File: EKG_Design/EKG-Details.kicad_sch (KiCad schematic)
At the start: 45 parts, among them J101 Conn_01x02_Pin, J102 Conn_01x02_Pin, J103 Conn_01x02_Pin, J104 Conn_01x03_Pin, J105 Conn_01x02_Pin, U101 OPA2156xDGK, U102 OPA2156xDGK, U103 INA826AIDR_/_SOIC8, U104 OPA2156xDGK, U105 OPA2156xDGK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

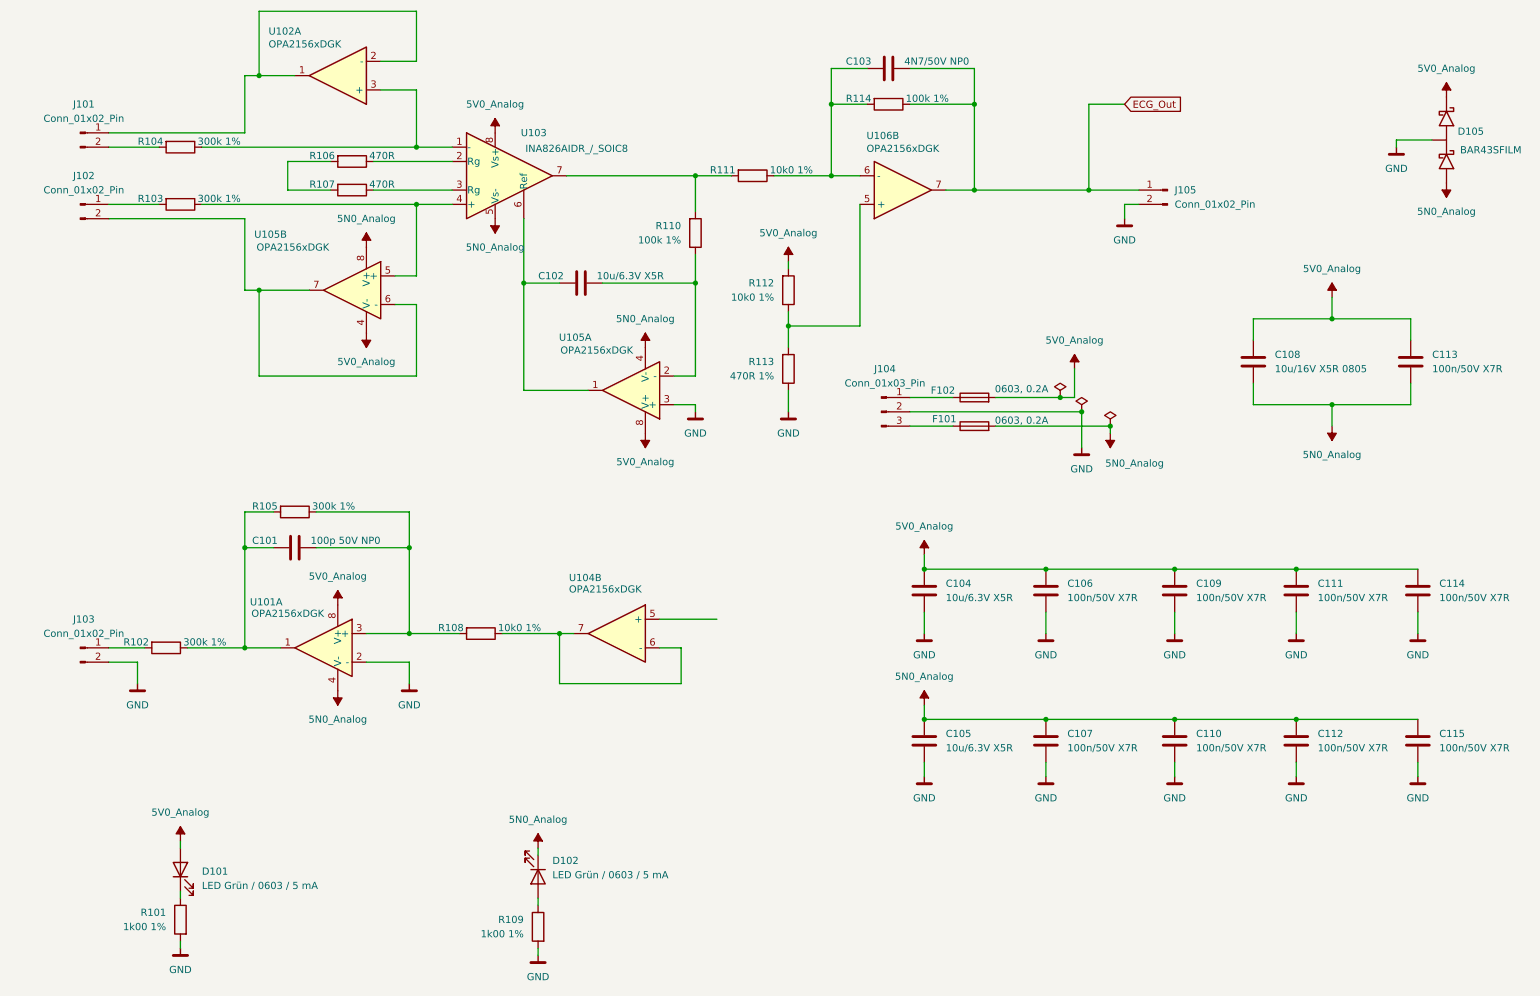
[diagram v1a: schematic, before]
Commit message: Finished ECG Schematic and finished laying out the PCB
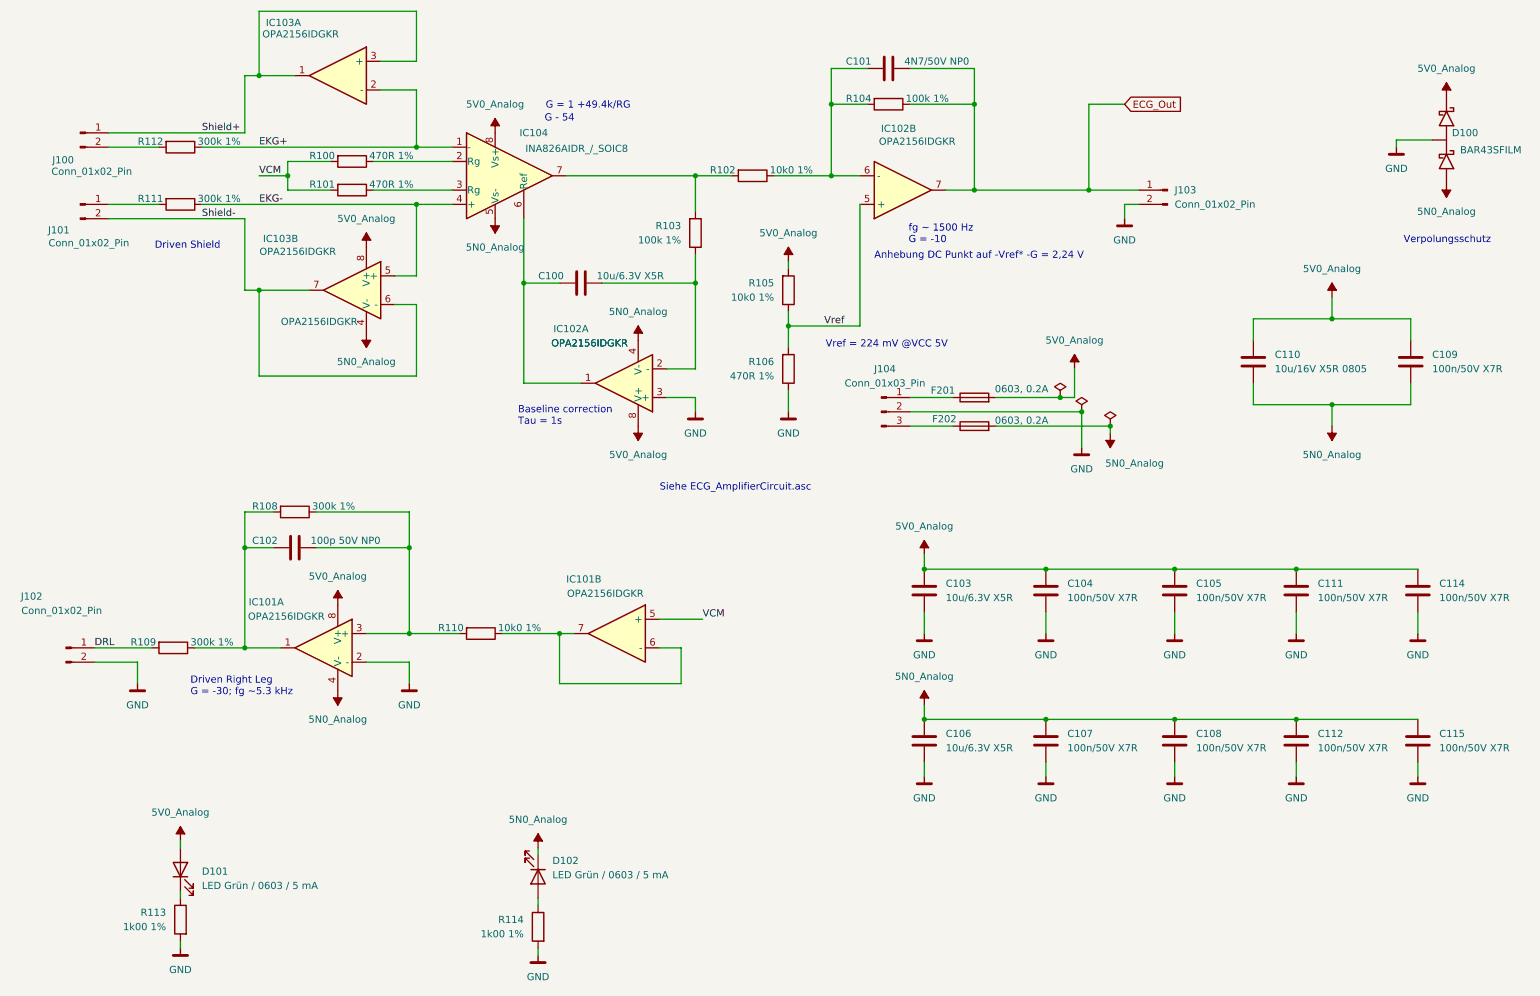
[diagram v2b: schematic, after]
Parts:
- removed unit 3 of U101
- removed unit 3 of U102
- removed U104, U106: OPA2156xDGK, Package_SO:VSSOP-8_3x3mm_P0.65mm, symbol Amplifier_Operational:OPA2156xDGK
- removed unit 3 of U105
- removed unit 2 of U105
- C100: renamed from C102; footprint (none) -> Capacitor_SMD:C_0603_1608Metric_Pad1.08x0.95mm_HandSolder
- C101: renamed from C103; footprint (none) -> Capacitor_SMD:C_0603_1608Metric_Pad1.08x0.95mm_HandSolder
- C102: renamed from C101; footprint (none) -> Capacitor_SMD:C_0603_1608Metric_Pad1.08x0.95mm_HandSolder
- C103: renamed from C104; footprint (none) -> Capacitor_SMD:C_0603_1608Metric_Pad1.08x0.95mm_HandSolder
- C104: renamed from C106; footprint (none) -> Capacitor_SMD:C_0603_1608Metric_Pad1.08x0.95mm_HandSolder
- C105: renamed from C109; footprint (none) -> Capacitor_SMD:C_0603_1608Metric_Pad1.08x0.95mm_HandSolder
- C106: renamed from C105; footprint (none) -> Capacitor_SMD:C_0603_1608Metric_Pad1.08x0.95mm_HandSolder
- C107, C111, C112, C114, C115: footprint (none) -> Capacitor_SMD:C_0603_1608Metric_Pad1.08x0.95mm_HandSolder
- C108: renamed from C110; footprint (none) -> Capacitor_SMD:C_0603_1608Metric_Pad1.08x0.95mm_HandSolder
- C109: renamed from C113; footprint (none) -> Capacitor_SMD:C_0603_1608Metric_Pad1.08x0.95mm_HandSolder
- C110: renamed from C108; footprint (none) -> Capacitor_SMD:C_0603_1608Metric_Pad1.08x0.95mm_HandSolder
- D101, D102: footprint (none) -> LED_SMD:LED_0603_1608Metric_Pad1.05x0.95mm_HandSolder
- F201: renamed from F102; footprint (none) -> Fuse:Fuse_0603_1608Metric_Pad1.05x0.95mm_HandSolder
- F202: renamed from F101; footprint (none) -> Fuse:Fuse_0603_1608Metric_Pad1.05x0.95mm_HandSolder
- IC101: renamed from U101; value OPA2156xDGK -> OPA2156IDGKR
- IC102: renamed from U105; value OPA2156xDGK -> OPA2156IDGKR
- IC103: renamed from U102; value OPA2156xDGK -> OPA2156IDGKR
- J100: renamed from J101; footprint (none) -> Connector_PinHeader_2.54mm:PinHeader_1x02_P2.54mm_Vertical
- J101: renamed from J102; footprint (none) -> Connector_PinHeader_2.54mm:PinHeader_1x02_P2.54mm_Vertical
- J102: renamed from J103; footprint (none) -> Connector_PinHeader_2.54mm:PinHeader_1x02_P2.54mm_Vertical
- J103: renamed from J105; footprint (none) -> Connector_PinHeader_2.54mm:PinHeader_1x02_P2.54mm_Vertical
- J104: footprint (none) -> Connector_PinHeader_2.54mm:PinHeader_1x03_P2.54mm_Vertical
- R100: renamed from R106; value 470R -> 470R 1%; footprint (none) -> Resistor_SMD:R_0603_1608Metric_Pad0.98x0.95mm_HandSolder
- R101: renamed from R107; value 470R -> 470R 1%; footprint (none) -> Resistor_SMD:R_0603_1608Metric_Pad0.98x0.95mm_HandSolder
- R102: renamed from R111; footprint (none) -> Resistor_SMD:R_0603_1608Metric_Pad0.98x0.95mm_HandSolder
- R103: renamed from R110; footprint (none) -> Resistor_SMD:R_0603_1608Metric_Pad0.98x0.95mm_HandSolder
- R104: renamed from R114; footprint (none) -> Resistor_SMD:R_0603_1608Metric_Pad0.98x0.95mm_HandSolder
- R105: renamed from R112; footprint (none) -> Resistor_SMD:R_0603_1608Metric_Pad0.98x0.95mm_HandSolder
- R106: renamed from R113; footprint (none) -> Resistor_SMD:R_0603_1608Metric_Pad0.98x0.95mm_HandSolder
- R108: renamed from R105; footprint (none) -> Resistor_SMD:R_0603_1608Metric_Pad0.98x0.95mm_HandSolder
- R109: renamed from R102; footprint (none) -> Resistor_SMD:R_0603_1608Metric_Pad0.98x0.95mm_HandSolder
- R110: renamed from R108; footprint (none) -> Resistor_SMD:R_0603_1608Metric_Pad0.98x0.95mm_HandSolder
- R111: renamed from R103; footprint (none) -> Resistor_SMD:R_0603_1608Metric_Pad0.98x0.95mm_HandSolder
- R112: renamed from R104; footprint (none) -> Resistor_SMD:R_0603_1608Metric_Pad0.98x0.95mm_HandSolder
- R113: renamed from R101; footprint (none) -> Resistor_SMD:R_0603_1608Metric_Pad0.98x0.95mm_HandSolder
- R114: renamed from R109; footprint (none) -> Resistor_SMD:R_0603_1608Metric_Pad0.98x0.95mm_HandSolder
- renumbered D105 to D100, U103 to IC104
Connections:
- net 5N0_Analog: now also IC101.4 (V-), IC102.4 (V-), IC103.4 (V-)
- net 5V0_Analog: now also IC101.8 (V+), IC102.8 (V+), IC103.8 (V+)
- net ECG_Out: now also IC102.7
- net GND: now also D100.2 (B); no longer D100.1 (A)
- net at C101.2, R102.1, R104.2: now also IC102.6 (-)
- net Shield+: now reaches IC103.1, J100.1 (Pin_1)
- net Shield+: now also IC103.3 (+); no longer IC103.2 (-)
- net EKG+: now reaches IC104.1 (-), R112.1
- net EKG+: now also IC103.2 (-); no longer IC103.3 (+)
- net DRL: now reaches J102.1 (Pin_1), R109.2
- net Vref: now reaches R105.1, R106.2
- net Vref: now also IC102.5 (+)
- net EKG-: now reaches IC104.4 (+), R111.1
- net EKG-: now also IC103.5 (+)
- net Shield-: now reaches J101.2 (Pin_2)
- net Shield-: now also IC103.6 (-), IC103.7
- net VCM: now reaches R100.2, R101.2
- net VCM: now also IC101.5 (+)
- net at R110.1: now also IC101.6 (-), IC101.7
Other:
- note added: "Anhebung DC Punkt auf -Vref* -G = 2,24 V"
- note added: "Baseline correction Tau = 1s"
- note added: "Driven Right Leg G = -30; fg ~5.3 kHz"
- note added: "Driven Shield"
- note added: "G - 54"
- note added: "G = 1 +49.4k/RG"
- note added: "Siehe ECG_AmplifierCircuit.asc"
- note added: "Verpolungsschutz"
- note added: "Vref = 224 mV @VCC 5V"
- note added: "fg ~ 1500 Hz G = -10"
- moved on the sheet: IC101B, IC102B, IC103A, J102, R109

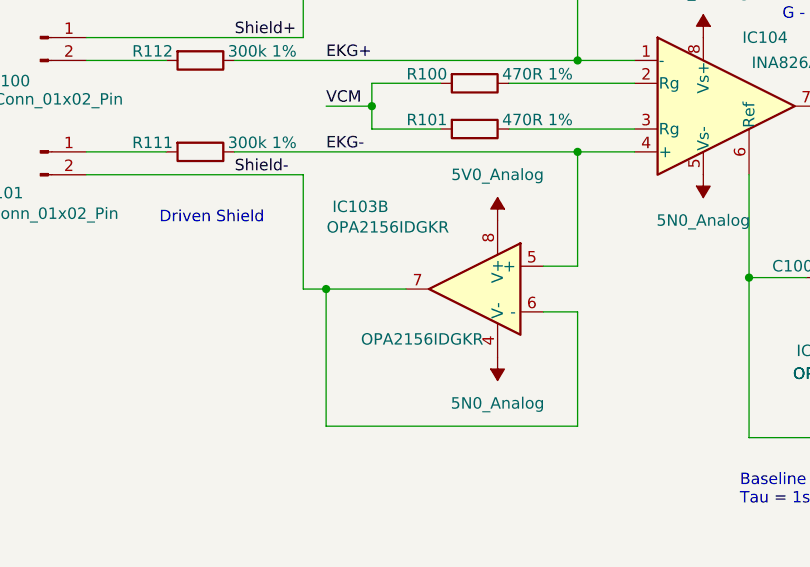
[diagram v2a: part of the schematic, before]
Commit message: adjusted board properties and added manifest items
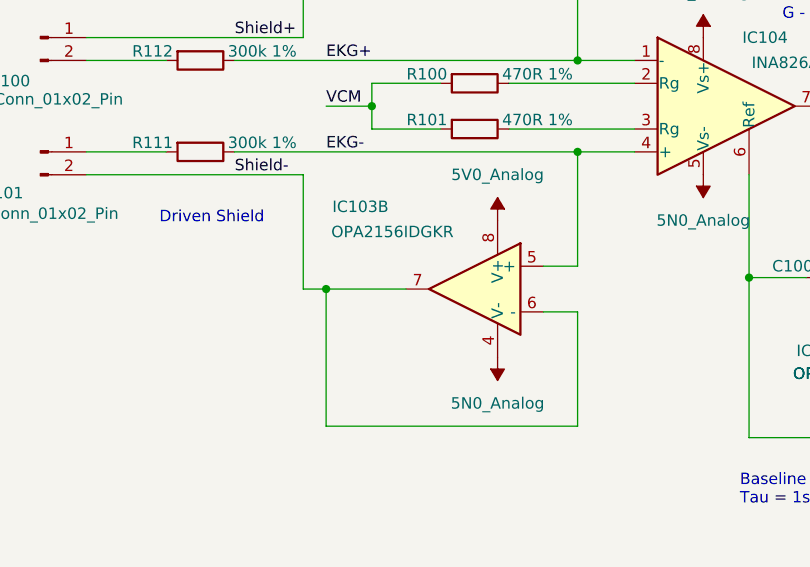
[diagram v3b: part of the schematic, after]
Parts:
- added unit 2 of IC101
- added unit 1 of IC101
- added unit 3 of IC102
- added unit 1 of IC102
- added unit 3 of IC103
- added unit 2 of IC103
- C100, C103, C106: manf# (none) -> CL10A106KQ8NNNC
- C101: manf# (none) -> GRM1885C1H472JA01D
- C102: manf# (none) -> GCM1885C2A101JA16D
- C104, C105, C107, C108, C109, C111, C112, C114, C115: manf# (none) -> MT18B104K500CT
- C110: manf# (none) -> EMK212BJ106KG-T
- D100: manf# (none) -> BAR43SFILM
- D101, D102: manf# (none) -> KT EELP41.12-S2U1-25-2X4X-5-R18
- F201, F202: manf# (none) -> FCC16201ABTP
- IC101, IC102, IC103: manf# (none) -> OPA2156IDGKR
- IC104: manf# (none) -> INA826AIDR
- J100, J101, J102, J103: manf# (none) -> 861400021YO10LF
- J104: manf# (none) -> G800W305018EU
- R100, R101, R106: manf# (none) -> ERJ-3EKF4700V
- R102, R105, R110: manf# (none) -> ERJ-3EKF1002V
- R103, R104: manf# (none) -> RR0816P-104-D
- R108, R109, R111, R112: manf# (none) -> CRCW0603300KFKEAC
- R113, R114: manf# (none) -> RK73H1JTTDD1001F
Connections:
- net 5N0_Analog: now also IC102.4 (V-), IC103.4 (V-); no longer IC102.4 (V-), IC103.4 (V-)
- net 5V0_Analog: now also IC102.8 (V+), IC103.8 (V+); no longer IC102.8 (V+), IC103.8 (V+)
- net EKG-: now also IC103.5 (+); no longer IC103.5 (+)
- net GND: now also IC101.2 (-), IC102.3 (+); no longer IC101.2 (-), IC102.3 (+)
- net Shield-: now also IC103.6 (-), IC103.7; no longer IC103.6 (-), IC103.7
- net VCM: now also IC101.5 (+); no longer IC101.5 (+)
- net at C102.2, R108.2, R109.1: now also IC101.1; no longer IC101.1
- net at C100.1, R103.1: now also IC102.2 (-); no longer IC102.2 (-)
- net at C100.2, IC104.6 (Ref): now also IC102.1; no longer IC102.1
- net at C102.1, R108.1, R110.2: now also IC101.3 (+); no longer IC101.3 (+)
- new net: IC101.6 (-), IC101.7, R110.1
